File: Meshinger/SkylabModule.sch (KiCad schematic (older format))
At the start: 6 parts, among them J1 Conn_02x06_Odd_Even, J2 Micro_SD_Card, J4 Conn_02x01, Q2 NTR2101P, U1 SKW92A, U2 BBQ10KBD

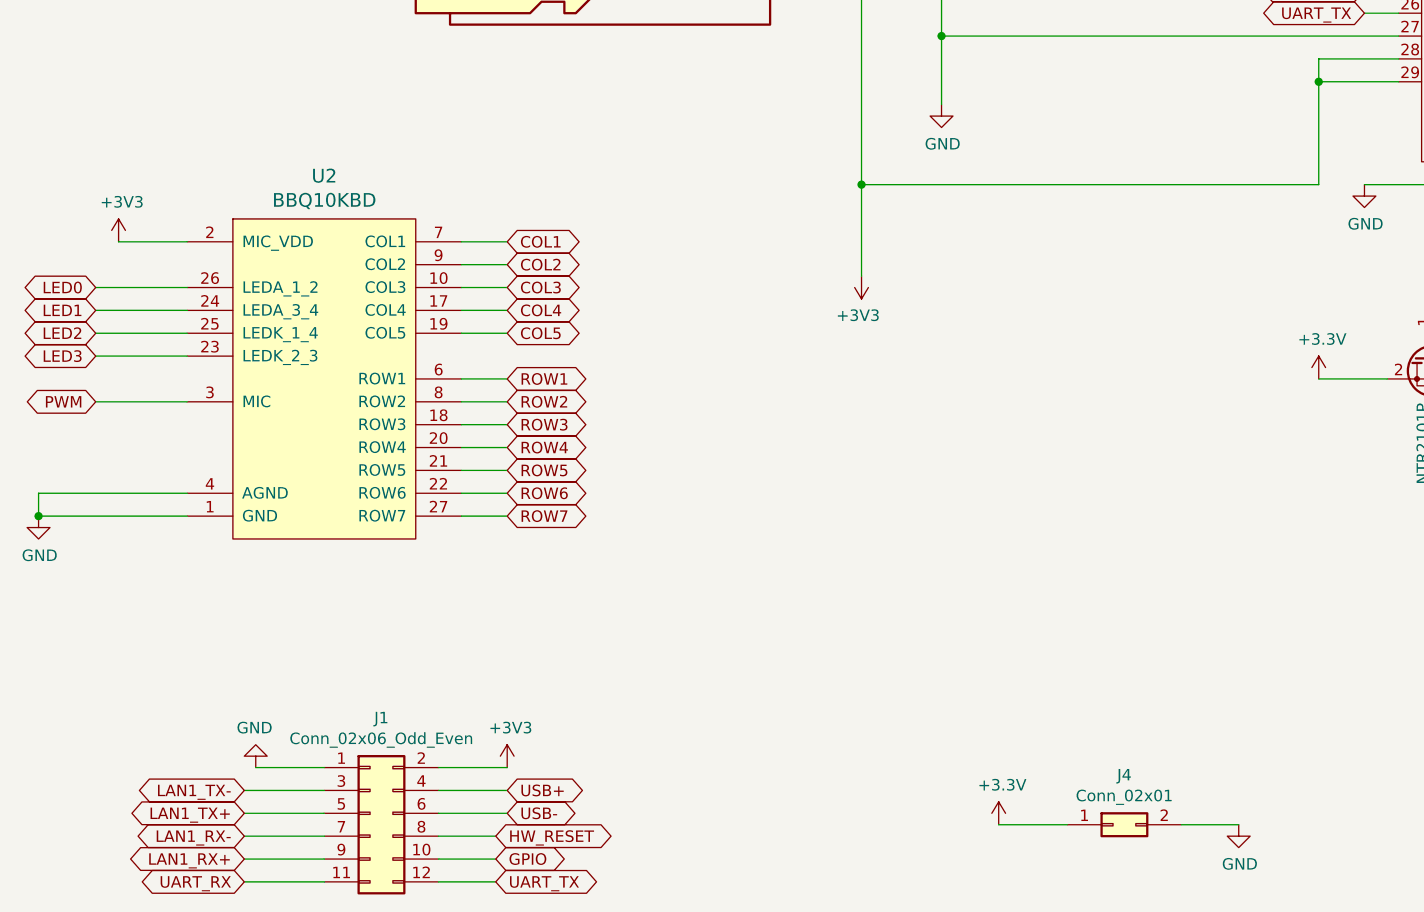
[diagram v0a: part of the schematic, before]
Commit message: Meshinger 1.0 rev B WARNING THE DC PLUG PINS ARE WRONG, SHORTS BATTERY!
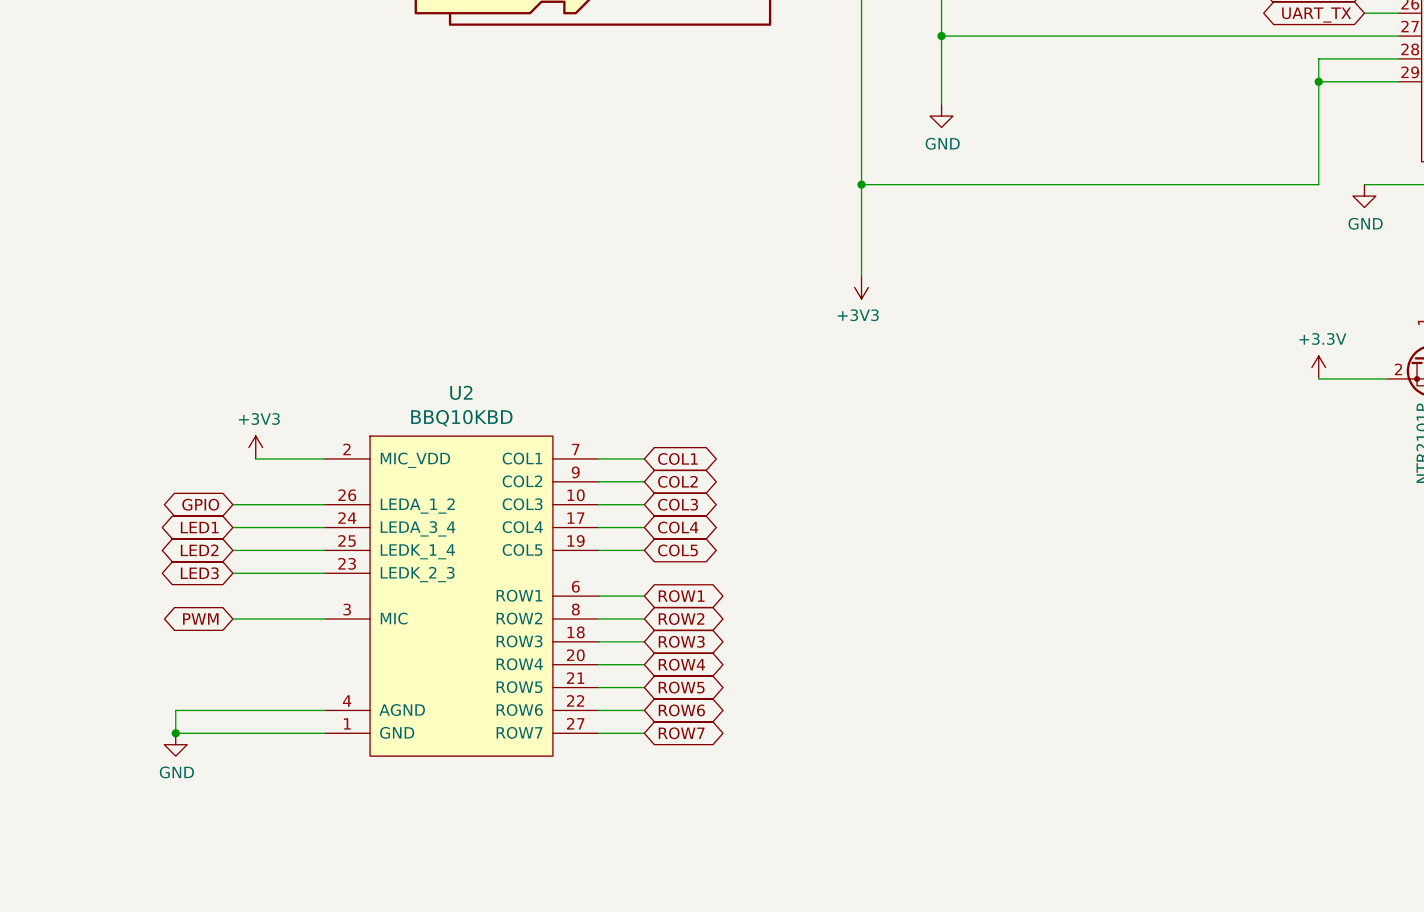
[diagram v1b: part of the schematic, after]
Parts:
- removed J1: Conn_02x06_Odd_Even, Connector_PinHeader_2.54mm:PinHeader_2x06_P2.54mm_Vertical, symbol Connector_Generic:Conn_02x06_Odd_Even
- removed J4: Conn_02x01, Connector_PinHeader_2.54mm:PinHeader_2x01_P2.54mm_Vertical, symbol Connector_Generic:Conn_02x01
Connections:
- net GPIO: now also U2.26 (LEDA_1_2)
- net LED0: no longer U2.26 (LEDA_1_2)
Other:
- moved on the sheet: U2
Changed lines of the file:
@@
 $Descr A4 11693 8268
 encoding utf-8
-Sheet 3 3
+Sheet 3 4
 Title ""
 Date ""
@@
 Wire Wire Line
 	8600 700  8600 2500
-$Comp
-L power:GND #PWR0114
-U 1 1 6043F178
-P 1950 6850
-F 0 "#PWR0114" H 1950 6600 50  0001 C CNN
-F 1 "GND" H 1955 6677 50  0000 C CNN
-F 2 "" H 1950 6850 50  0001 C CNN
-F 3 "" H 1950 6850 50  0001 C CNN
-	1    1950 6850
-	-1   0    0    1
-$EndComp
-Text GLabel 1900 7350 0    50   BiDi ~ 0
-UART_RX
-Text GLabel 3000 7350 2    50   BiDi ~ 0
-UART_TX
-Wire Wire Line
-	1950 6850 2250 6850
-Wire Wire Line
-	2750 6850 3050 6850
 Text GLabel 6800 3450 0    50   BiDi ~ 0
 UART_RX
@@
 Wire Wire Line
 	7900 2200 7650 2200
-Text GLabel 3050 6950 2    50   BiDi ~ 0
-USB+
-Text GLabel 3050 7050 2    50   BiDi ~ 0
-USB-
-Wire Wire Line
-	2750 6950 3050 6950
-Wire Wire Line
-	2750 7050 3050 7050
 Text GLabel 9300 1750 2    50   BiDi ~ 0
 LAN1_TX-
@@
 Wire Wire Line
 	9300 1750 9300 2500
-Text GLabel 1900 7250 0    50   BiDi ~ 0
-LAN1_RX+
-Text GLabel 1900 7150 0    50   BiDi ~ 0
-LAN1_RX-
-Text GLabel 1900 7050 0    50   BiDi ~ 0
-LAN1_TX+
-Text GLabel 1900 6950 0    50   BiDi ~ 0
-LAN1_TX-
-Wire Wire Line
-	1900 7150 2250 7150
-Wire Wire Line
-	1900 7250 2250 7250
-Wire Wire Line
-	2750 7150 3000 7150
-Wire Wire Line
-	2750 7250 3000 7250
 Wire Wire Line
 	9500 4300 9500 4600
@@
 L Keyboard:BBQ10KBD U2
 U 1 1 60461E86
-P 2250 5150
-F 0 "U2" H 2250 6037 60  0000 C CNN
-F 1 "BBQ10KBD" H 2250 5931 60  0000 C CNN
-F 2 "BBQ10KBD:BM14B(0.8)-24DS-0.4V(53)" H 2250 5931 60  0001 C CNN
-F 3 "" H 2250 4800 60  0001 C CNN
-	1    2250 5150
+P 2850 6100
+F 0 "U2" H 2850 6987 60  0000 C CNN
+F 1 "BBQ10KBD" H 2850 6881 60  0000 C CNN
+F 2 "BBQ10KBD:BM14B(0.8)-24DS-0.4V(53)" H 2850 6881 60  0001 C CNN
+F 3 "" H 2850 5750 60  0001 C CNN
+	1    2850 6100
 	1    0    0    -1
 $EndComp
@@
 L power:GND #PWR0116
 U 1 1 60465DD2
-P 1000 5750
-F 0 "#PWR0116" H 1000 5500 50  0001 C CNN
-F 1 "GND" H 1005 5577 50  0000 C CNN
-F 2 "" H 1000 5750 50  0001 C CNN
-F 3 "" H 1000 5750 50  0001 C CNN
-	1    1000 5750
-	1    0    0    -1
-$EndComp
-Wire Wire Line
-	1650 5650 1000 5650
-Wire Wire Line
-	1000 5650 1000 5750
-Wire Wire Line
-	1650 5750 1000 5750
-Connection ~ 1000 5750
+P 1600 6700
+F 0 "#PWR0116" H 1600 6450 50  0001 C CNN
+F 1 "GND" H 1605 6527 50  0000 C CNN
+F 2 "" H 1600 6700 50  0001 C CNN
+F 3 "" H 1600 6700 50  0001 C CNN
+	1    1600 6700
+	1    0    0    -1
+$EndComp
+Wire Wire Line
+	2250 6600 1600 6600
+Wire Wire Line
+	1600 6600 1600 6700
+Wire Wire Line
+	2250 6700 1600 6700
+Connection ~ 1600 6700
 $Comp
 L power:+3V3 #PWR0117
 U 1 1 6046A3A4
-P 1350 4550
-F 0 "#PWR0117" H 1350 4400 50  0001 C CNN
-F 1 "+3V3" H 1365 4723 50  0000 C CNN
-F 2 "" H 1350 4550 50  0001 C CNN
-F 3 "" H 1350 4550 50  0001 C CNN
-	1    1350 4550
-	1    0    0    -1
-$EndComp
-Wire Wire Line
-	1350 4550 1650 4550
-Text GLabel 1250 5250 0    50   BiDi ~ 0
+P 1950 5500
+F 0 "#PWR0117" H 1950 5350 50  0001 C CNN
+F 1 "+3V3" H 1965 5673 50  0000 C CNN
+F 2 "" H 1950 5500 50  0001 C CNN
+F 3 "" H 1950 5500 50  0001 C CNN
+	1    1950 5500
+	1    0    0    -1
+$EndComp
+Wire Wire Line
+	1950 5500 2250 5500
+Text GLabel 1850 6200 0    50   BiDi ~ 0
 PWM
 Wire Wire Line
-	1250 5250 1650 5250
-Text GLabel 3050 4550 2    50   BiDi ~ 0
+	1850 6200 2250 6200
+Text GLabel 3650 5500 2    50   BiDi ~ 0
 COL1
-Text GLabel 3050 4650 2    50   BiDi ~ 0
+Text GLabel 3650 5600 2    50   BiDi ~ 0
 COL2
-Text GLabel 3050 4750 2    50   BiDi ~ 0
+Text GLabel 3650 5700 2    50   BiDi ~ 0
 COL3
-Text GLabel 3050 4850 2    50   BiDi ~ 0
+Text GLabel 3650 5800 2    50   BiDi ~ 0
 COL4
-Text GLabel 3050 4950 2    50   BiDi ~ 0
+Text GLabel 3650 5900 2    50   BiDi ~ 0
 COL5
-Text GLabel 3050 5150 2    50   BiDi ~ 0
+Text GLabel 3650 6100 2    50   BiDi ~ 0
 ROW1
-Text GLabel 3050 5250 2    50   BiDi ~ 0
+Text GLabel 3650 6200 2    50   BiDi ~ 0
 ROW2
-Text GLabel 3050 5350 2    50   BiDi ~ 0
+Text GLabel 3650 6300 2    50   BiDi ~ 0
 ROW3
-Text GLabel 3050 5450 2    50   BiDi ~ 0
+Text GLabel 3650 6400 2    50   BiDi ~ 0
 ROW4
-Text GLabel 3050 5550 2    50   BiDi ~ 0
+Text GLabel 3650 6500 2    50   BiDi ~ 0
 ROW5
-Text GLabel 3050 5650 2    50   BiDi ~ 0
+Text GLabel 3650 6600 2    50   BiDi ~ 0
 ROW6
-Text GLabel 3050 5750 2    50   BiDi ~ 0
+Text GLabel 3650 6700 2    50   BiDi ~ 0
 ROW7
 Wire Wire Line
-	2850 4550 3050 4550
-Wire Wire Line
-	2850 4650 3050 4650
-Wire Wire Line
-	2850 4750 3050 4750
-Wire Wire Line
-	2850 4850 3050 4850
-Wire Wire Line
-	2850 4950 3050 4950
-Wire Wire Line
-	2850 5150 3050 5150
-Wire Wire Line
-	2850 5250 3050 5250
-Wire Wire Line
-	2850 5350 3050 5350
-Wire Wire Line
-	2850 5450 3050 5450
-Wire Wire Line
-	2850 5550 3050 5550
-Wire Wire Line
-	2850 5650 3050 5650
-Wire Wire Line
-	2850 5750 3050 5750
-Text GLabel 1250 4750 0    50   BiDi ~ 0
-LED0
-Text GLabel 1250 4850 0    50   BiDi ~ 0
+	3450 5500 3650 5500
+Wire Wire Line
+	3450 5600 3650 5600
+Wire Wire Line
+	3450 5700 3650 5700
+Wire Wire Line
+	3450 5800 3650 5800
+Wire Wire Line
+	3450 5900 3650 5900
+Wire Wire Line
+	3450 6100 3650 6100
+Wire Wire Line
+	3450 6200 3650 6200
+Wire Wire Line
+	3450 6300 3650 6300
+Wire Wire Line
+	3450 6400 3650 6400
+Wire Wire Line
+	3450 6500 3650 6500
+Wire Wire Line
+	3450 6600 3650 6600
+Wire Wire Line
+	3450 6700 3650 6700
+Text GLabel 1850 5700 0    50   BiDi ~ 0
+GPIO
+Text GLabel 1850 5800 0    50   BiDi ~ 0
 LED1
-Text GLabel 1250 4950 0    50   BiDi ~ 0
+Text GLabel 1850 5900 0    50   BiDi ~ 0
 LED2
-Text GLabel 1250 5050 0    50   BiDi ~ 0
+Text GLabel 1850 6000 0    50   BiDi ~ 0
 LED3
 Wire Wire Line
-	1250 4750 1650 4750
-Wire Wire Line
-	1250 4850 1650 4850
-Wire Wire Line
-	1250 4950 1650 4950
-Wire Wire Line
-	1250 5050 1650 5050
-Wire Wire Line
-	1900 7350 2250 7350
+	1850 5700 2250 5700
+Wire Wire Line
+	1850 5800 2250 5800
+Wire Wire Line
+	1850 5900 2250 5900
+Wire Wire Line
+	1850 6000 2250 6000
 Text GLabel 8300 4850 0    50   BiDi ~ 0
 LED0
@@
 Wire Wire Line
 	9600 4300 9600 4450
-Wire Wire Line
-	1900 6950 2250 6950
-Text GLabel 3000 7150 2    50   BiDi ~ 0
-HW_RESET
-Wire Wire Line
-	2750 7350 3000 7350
-$Comp
-L power:+3V3 #PWR0118
-U 1 1 60540926
-P 3050 6850
-F 0 "#PWR0118" H 3050 6700 50  0001 C CNN
-F 1 "+3V3" H 3065 7023 50  0000 C CNN
-F 2 "" H 3050 6850 50  0001 C CNN
-F 3 "" H 3050 6850 50  0001 C CNN
-	1    3050 6850
-	1    0    0    -1
-$EndComp
-Wire Wire Line
-	2250 7050 1900 7050
 Text GLabel 9300 4900 2    50   BiDi ~ 0
 HW_RESET
 Wire Wire Line
 	9300 4300 9300 4900
-$Comp
-L Connector_Generic:Conn_02x06_Odd_Even J1
-U 1 1 603D8DA8
-P 2450 7050
-F 0 "J1" H 2500 7467 50  0000 C CNN
-F 1 "Conn_02x06_Odd_Even" H 2500 7376 50  0000 C CNN
-F 2 "Connector_PinHeader_2.54mm:PinHeader_2x06_P2.54mm_Vertical" H 2450 7050 50  0001 C CNN
-F 3 "~" H 2450 7050 50  0001 C CNN
-	1    2450 7050
-	1    0    0    -1
-$EndComp
 Text GLabel 9400 4750 2    50   BiDi ~ 0
 GPIO
@@
 Wire Wire Line
 	7750 5150 7300 5150
-Text GLabel 3000 7250 2    50   BiDi ~ 0
-GPIO
-$Comp
-L Connector_Generic:Conn_02x01 J4
-U 1 1 6040B2A9
-P 5700 7100
-F 0 "J4" H 5750 7317 50  0000 C CNN
-F 1 "Conn_02x01" H 5750 7226 50  0000 C CNN
-F 2 "Connector_PinHeader_2.54mm:PinHeader_2x01_P2.54mm_Vertical" H 5700 7100 50  0001 C CNN
-F 3 "~" H 5700 7100 50  0001 C CNN
-	1    5700 7100
-	1    0    0    -1
-$EndComp
-$Comp
-L power:+3.3V #PWR0102
-U 1 1 6040B8AE
-P 5200 7100
-F 0 "#PWR0102" H 5200 6950 50  0001 C CNN
-F 1 "+3.3V" H 5215 7273 50  0000 C CNN
-F 2 "" H 5200 7100 50  0001 C CNN
-F 3 "" H 5200 7100 50  0001 C CNN
-	1    5200 7100
-	1    0    0    -1
-$EndComp
-$Comp
-L power:GND #PWR0119
-U 1 1 6040F99A
-P 6250 7100
-F 0 "#PWR0119" H 6250 6850 50  0001 C CNN
-F 1 "GND" H 6255 6927 50  0000 C CNN
-F 2 "" H 6250 7100 50  0001 C CNN
-F 3 "" H 6250 7100 50  0001 C CNN
-	1    6250 7100
-	1    0    0    -1
-$EndComp
-Wire Wire Line
-	5200 7100 5500 7100
-Wire Wire Line
-	6000 7100 6250 7100
 Wire Wire Line
 	7900 4450 7100 4450

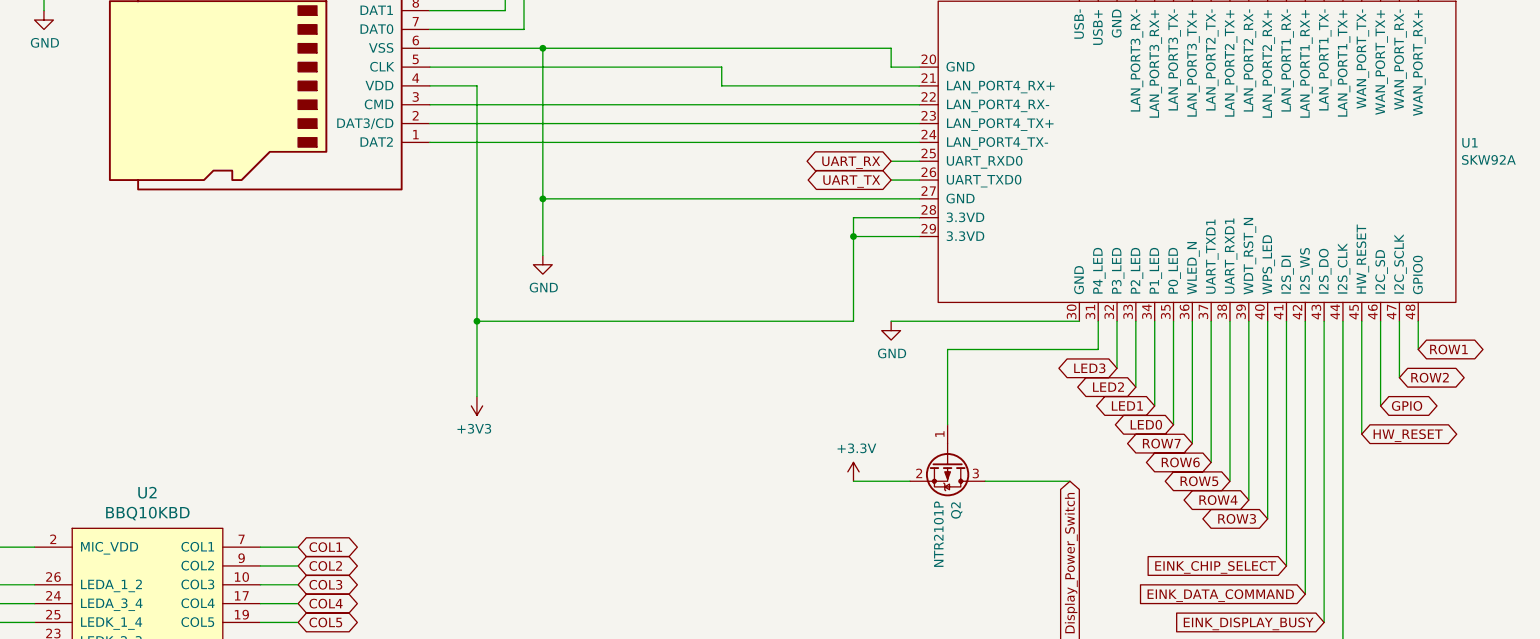
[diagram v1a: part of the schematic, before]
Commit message: Meshinger 1.0 rev C, Display Power MOSFET heats up while off...
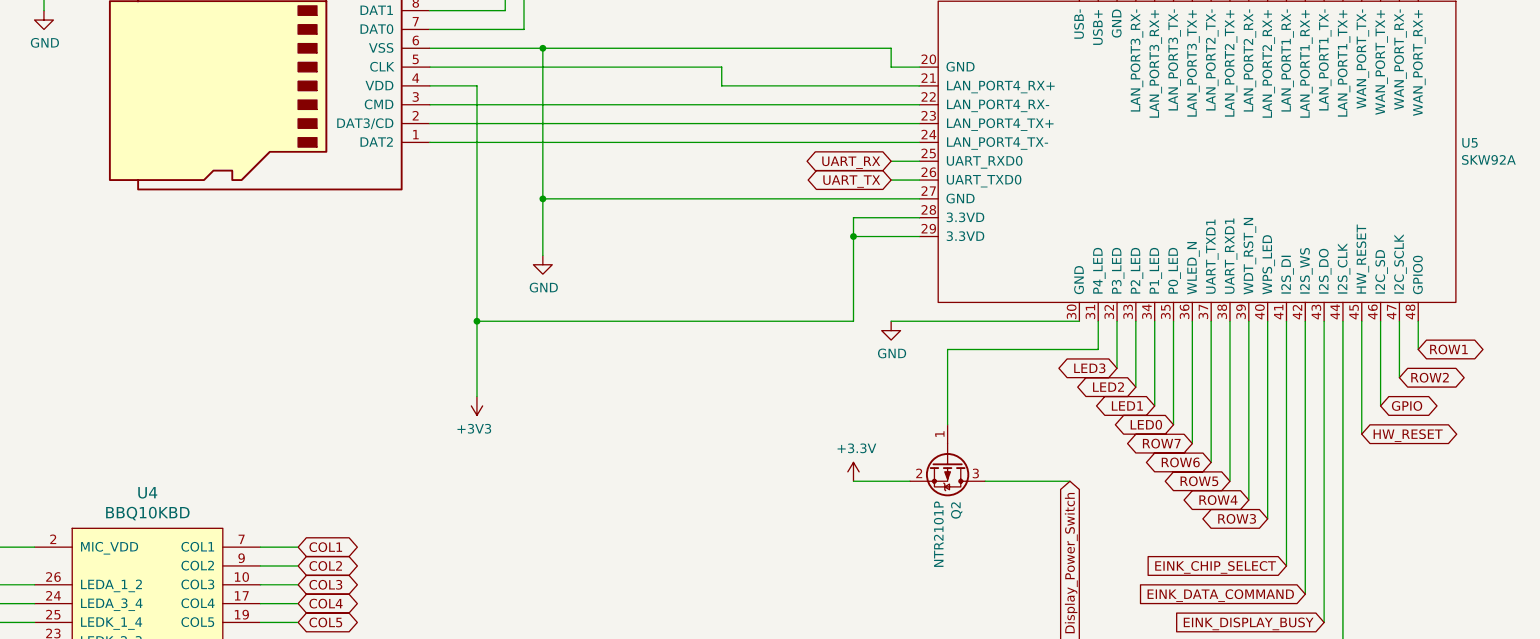
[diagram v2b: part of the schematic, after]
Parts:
- renumbered U2 to U4, U1 to U5
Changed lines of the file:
@@
 $EndDescr
 $Comp
-L SKW92A:SKW92A U1
+L SKW92A:SKW92A U5
 U 1 1 60415F24
 P 8400 3450
-F 0 "U1" H 9828 3546 50  0000 L CNN
+F 0 "U5" H 9828 3546 50  0000 L CNN
 F 1 "SKW92A" H 9828 3455 50  0000 L CNN
 F 2 "SKW92A:SKYLAB_SKW92A" H 9828 3455 50  0001 L CNN
@@
 $EndComp
 $Comp
-L power:GND #PWR0109
+L power:GND #PWR010
 U 1 1 6041EF30
 P 2300 2650
-F 0 "#PWR0109" H 2300 2400 50  0001 C CNN
+F 0 "#PWR010" H 2300 2400 50  0001 C CNN
 F 1 "GND" H 2305 2477 50  0000 C CNN
 F 2 "" H 2300 2650 50  0001 C CNN
@@
 	8200 1300 8200 2500
 $Comp
-L power:+3V3 #PWR0110
+L power:+3V3 #PWR011
 U 1 1 6042698A
 P 4600 4700
-F 0 "#PWR0110" H 4600 4550 50  0001 C CNN
+F 0 "#PWR011" H 4600 4550 50  0001 C CNN
 F 1 "+3V3" H 4615 4873 50  0000 C CNN
 F 2 "" H 4600 4700 50  0001 C CNN
@@
 	4600 3050 4600 4300
 $Comp
-L power:GND #PWR0111
+L power:GND #PWR012
 U 1 1 60427AAD
 P 4950 3950
-F 0 "#PWR0111" H 4950 3700 50  0001 C CNN
+F 0 "#PWR012" H 4950 3700 50  0001 C CNN
 F 1 "GND" H 4955 3777 50  0000 C CNN
 F 2 "" H 4950 3950 50  0001 C CNN
@@
 	4950 2850 4950 3650
 $Comp
-L power:GND #PWR0112
+L power:GND #PWR016
 U 1 1 60428695
 P 7900 1050
-F 0 "#PWR0112" H 7900 800 50  0001 C CNN
+F 0 "#PWR016" H 7900 800 50  0001 C CNN
 F 1 "GND" H 7905 877 50  0000 C CNN
 F 2 "" H 7900 1050 50  0001 C CNN
@@
 	6600 3850 6600 4300
 $Comp
-L power:GND #PWR0113
+L power:GND #PWR014
 U 1 1 6042D8F2
 P 6800 4300
-F 0 "#PWR0113" H 6800 4050 50  0001 C CNN
+F 0 "#PWR014" H 6800 4050 50  0001 C CNN
 F 1 "GND" H 6805 4127 50  0000 C CNN
 F 2 "" H 6800 4300 50  0001 C CNN
@@
 	6800 3550 6950 3550
 $Comp
-L power:GND #PWR0115
+L power:GND #PWR015
 U 1 1 60443BB1
 P 7800 1650
-F 0 "#PWR0115" H 7800 1400 50  0001 C CNN
+F 0 "#PWR015" H 7800 1400 50  0001 C CNN
 F 1 "GND" H 7805 1477 50  0000 C CNN
 F 2 "" H 7800 1650 50  0001 C CNN
@@
 	9400 4300 9400 4750
 $Comp
-L Keyboard:BBQ10KBD U2
+L Keyboard:BBQ10KBD U4
 U 1 1 60461E86
 P 2850 6100
-F 0 "U2" H 2850 6987 60  0000 C CNN
+F 0 "U4" H 2850 6987 60  0000 C CNN
 F 1 "BBQ10KBD" H 2850 6881 60  0000 C CNN
 F 2 "BBQ10KBD:BM14B(0.8)-24DS-0.4V(53)" H 2850 6881 60  0001 C CNN
@@
 PWM
 $Comp
-L power:GND #PWR0116
+L power:GND #PWR08
 U 1 1 60465DD2
 P 1600 6700
-F 0 "#PWR0116" H 1600 6450 50  0001 C CNN
+F 0 "#PWR08" H 1600 6450 50  0001 C CNN
 F 1 "GND" H 1605 6527 50  0000 C CNN
 F 2 "" H 1600 6700 50  0001 C CNN
@@
 Connection ~ 1600 6700
 $Comp
-L power:+3V3 #PWR0117
+L power:+3V3 #PWR09
 U 1 1 6046A3A4
 P 1950 5500
-F 0 "#PWR0117" H 1950 5350 50  0001 C CNN
+F 0 "#PWR09" H 1950 5350 50  0001 C CNN
 F 1 "+3V3" H 1965 5673 50  0000 C CNN
 F 2 "" H 1950 5500 50  0001 C CNN
@@
 $EndComp
 $Comp
-L power:+3.3V #PWR0120
+L power:+3.3V #PWR013
 U 1 1 603F3686
 P 6600 5150
-F 0 "#PWR0120" H 6600 5000 50  0001 C CNN
+F 0 "#PWR013" H 6600 5000 50  0001 C CNN
 F 1 "+3.3V" H 6615 5323 50  0000 C CNN
 F 2 "" H 6600 5150 50  0001 C CNN
